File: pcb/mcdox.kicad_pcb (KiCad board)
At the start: 2 copper layers, 39 x 46 mm, 5 parts

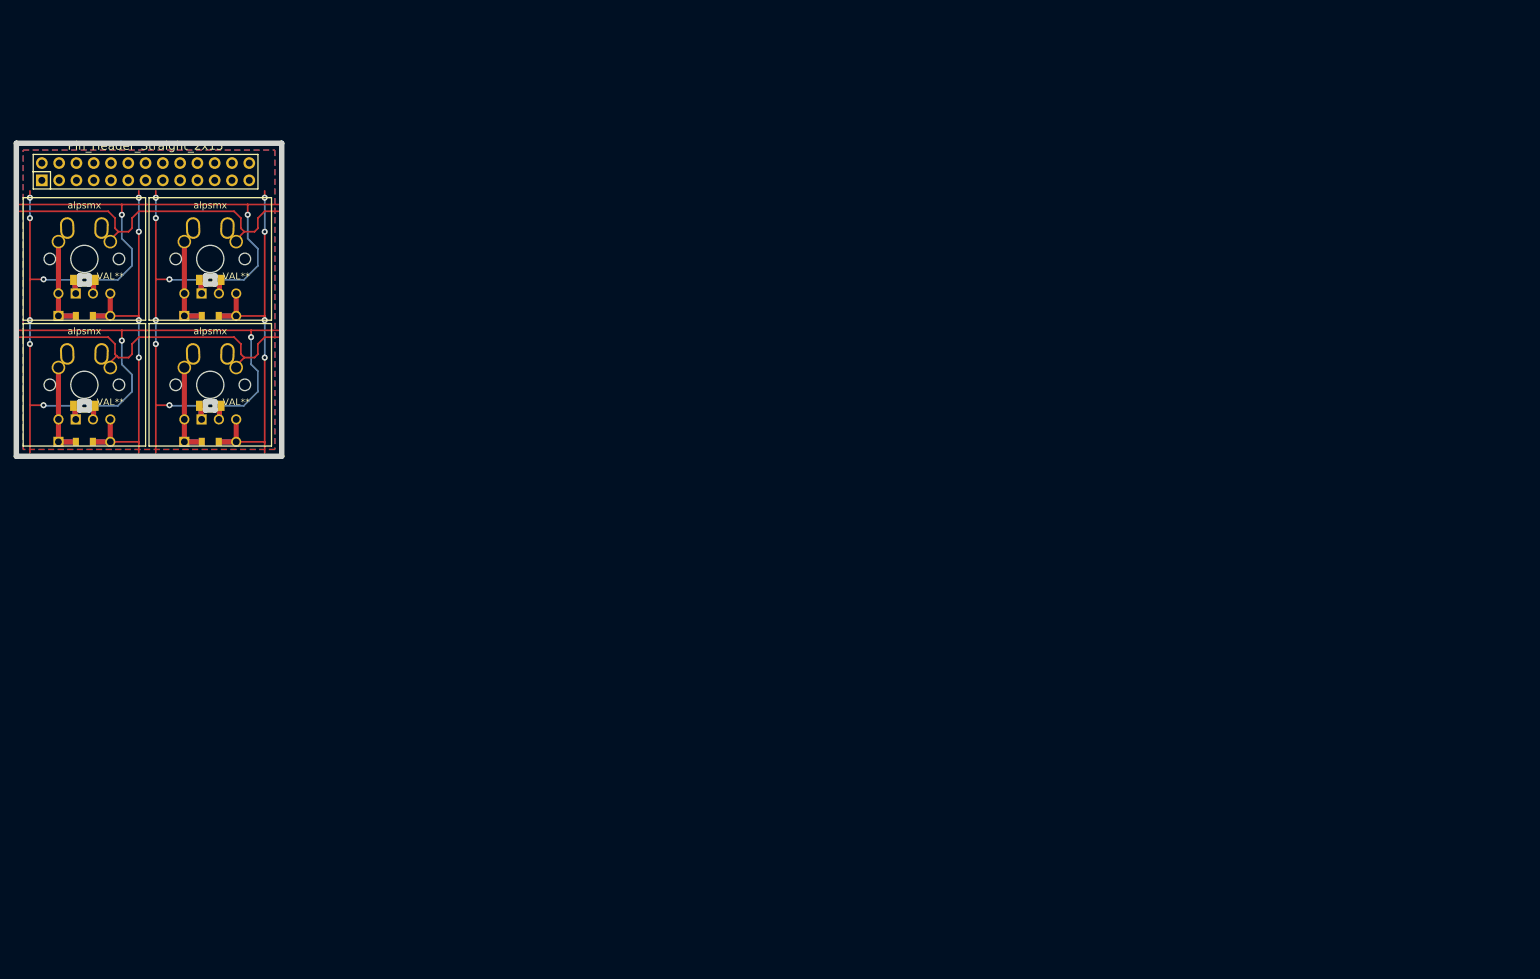
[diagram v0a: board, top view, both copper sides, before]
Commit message: First proper attempt at a full routing.
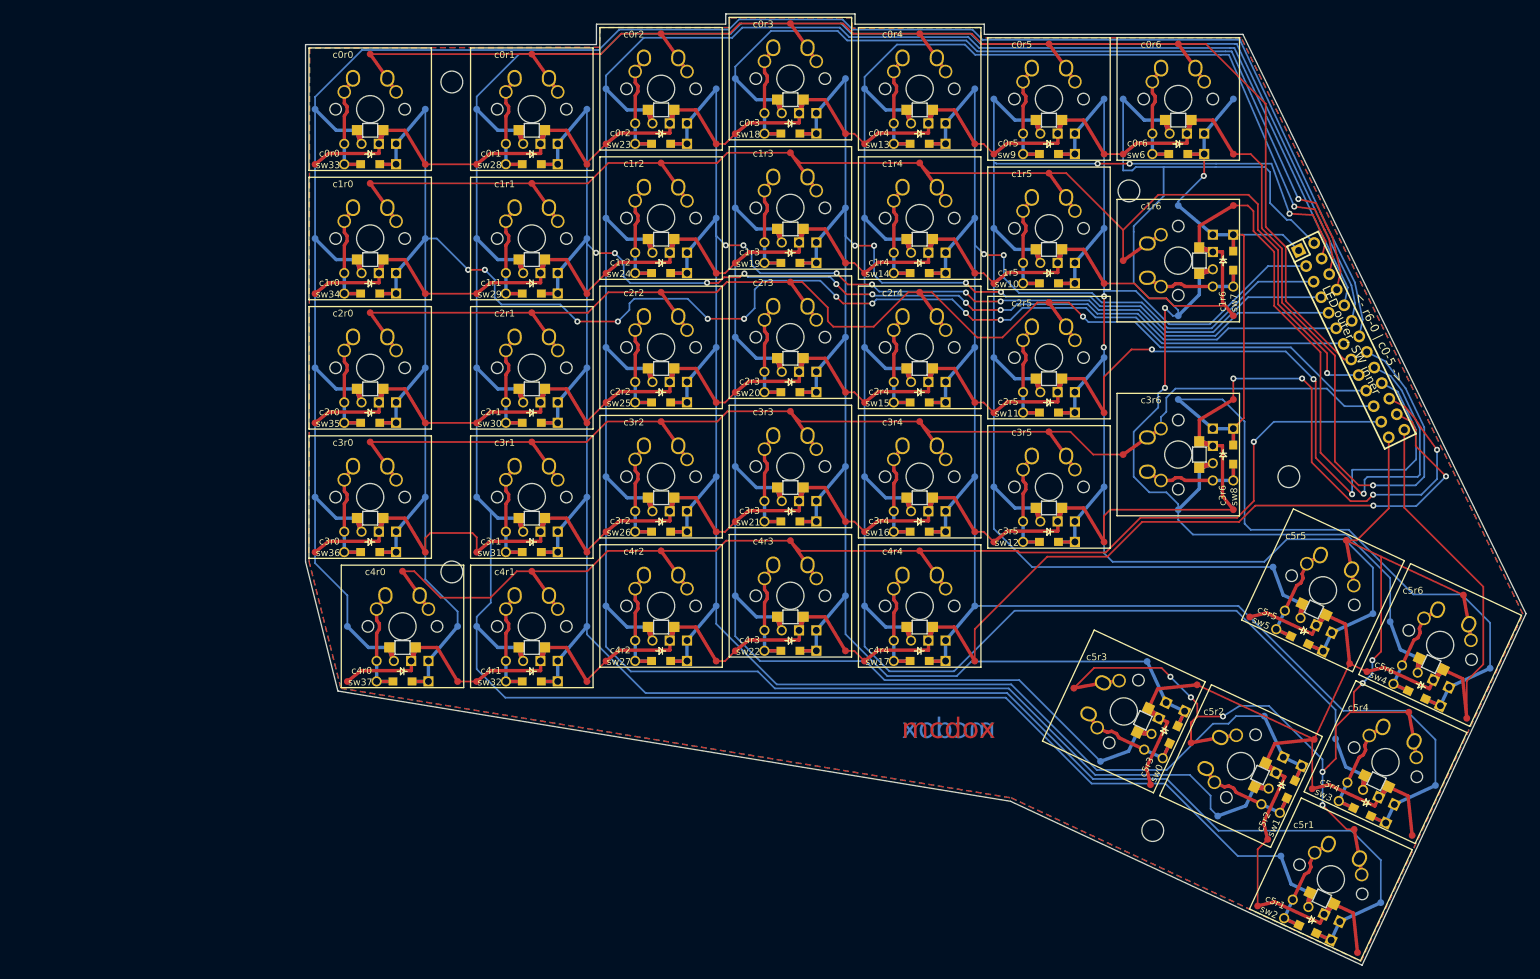
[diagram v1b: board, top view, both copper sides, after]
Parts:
- removed Pin_Header_Straight_2x13: Val**, Pin_Headers:Pin_Header_Straight_2x13
- removed alpsmx (x4): VAL**, mcdox:alpsmx
- added <- r6-0 | c0-5 ->: LED outer, SW inner, Pin_Header_Straight_2X13, F.Cu at (224.2, 67.9)
- added ?: , m3_hole, F.Cu at (92.0, 102.0)
- added ?: , m3_hole, F.Cu at (92.0, 30.0)
- added ?: , m3_hole, F.Cu at (191.5, 46.0)
- added ?: , m3_hole, F.Cu at (215.0, 88.0)
- added ?: , m3_hole, F.Cu at (195.0, 140.0)
- added sw0: c5r3, alpsmx, F.Cu at (190.8, 122.5)
- added sw1: c5r2, alpsmx, F.Cu at (208.0, 130.5)
- added sw10: c1r5, alpsmx, F.Cu at (179.8, 51.5)
- added sw11: c2r5, alpsmx, F.Cu at (179.8, 70.5)
- added sw12: c3r5, alpsmx, F.Cu at (179.8, 89.5)
- added sw13: c0r4, alpsmx, F.Cu at (160.8, 31.0)
- added sw14: c1r4, alpsmx, F.Cu at (160.8, 50.0)
- added sw15: c2r4, alpsmx, F.Cu at (160.8, 69.0)
- added sw16: c3r4, alpsmx, F.Cu at (160.8, 88.0)
- added sw17: c4r4, alpsmx, F.Cu at (160.8, 107.0)
- added sw18: c0r3, alpsmx, F.Cu at (141.8, 29.5)
- added sw19: c1r3, alpsmx, F.Cu at (141.8, 48.5)
- added sw2: c5r1, alpsmx, F.Cu at (221.2, 147.2)
- added sw20: c2r3, alpsmx, F.Cu at (141.8, 67.5)
- added sw21: c3r3, alpsmx, F.Cu at (141.8, 86.5)
- added sw22: c4r3, alpsmx, F.Cu at (141.8, 105.5)
- added sw23: c0r2, alpsmx, F.Cu at (122.8, 31.0)
- added sw24: c1r2, alpsmx, F.Cu at (122.8, 50.0)
- added sw25: c2r2, alpsmx, F.Cu at (122.8, 69.0)
- added sw26: c3r2, alpsmx, F.Cu at (122.8, 88.0)
- added sw27: c4r2, alpsmx, F.Cu at (122.8, 107.0)
- added sw28: c0r1, alpsmx, F.Cu at (103.8, 34.0)
- added sw29: c1r1, alpsmx, F.Cu at (103.8, 53.0)
- added sw3: c5r4, alpsmx, F.Cu at (229.2, 129.9)
- added sw30: c2r1, alpsmx, F.Cu at (103.8, 72.0)
- added sw31: c3r1, alpsmx, F.Cu at (103.8, 91.0)
- added sw32: c4r1, alpsmx, F.Cu at (103.8, 110.0)
- added sw33: c0r0, alpsmx, F.Cu at (80.0, 34.0)
- added sw34: c1r0, alpsmx, F.Cu at (80.0, 53.0)
- added sw35: c2r0, alpsmx, F.Cu at (80.0, 72.0)
- added sw36: c3r0, alpsmx, F.Cu at (80.0, 91.0)
- added sw37: c4r0, alpsmx, F.Cu at (84.8, 110.0)
- added sw4: c5r6, alpsmx, F.Cu at (237.2, 112.7)
- added sw5: c5r5, alpsmx, F.Cu at (220.0, 104.7)
- added sw6: c0r6, alpsmx, F.Cu at (198.8, 32.5)
- added sw7: c1r6, alpsmx, F.Cu at (198.8, 56.2)
- added sw8: c3r6, alpsmx, F.Cu at (198.8, 84.8)
- added sw9: c0r5, alpsmx, F.Cu at (179.8, 32.5)
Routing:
- net (no net): track 437.2 -> 5020.2 mm, vias 24 -> 61
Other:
- board size 39 x 46 mm -> 179.4 x 139.8 mm
- rule trace_min: 0.254 -> 0.5
- board text added: "c0r0"
- board text added: "c0r1"
- board text added: "c0r2"
- board text added: "c0r3"
- board text added: "c0r4"
- board text added: "c0r5"
- board text added: "c0r6"
- board text added: "c1r0"
- board text added: "c1r1"
- board text added: "c1r2"
- board text added: "c1r3"
- board text added: "c1r4"
- board text added: "c1r5"
- board text added: "c1r6"
- board text added: "c2r0"
- board text added: "c2r1"
- board text added: "c2r2"
- board text added: "c2r3"
- board text added: "c2r4"
- board text added: "c2r5"
- board text added: "c3r0"
- board text added: "c3r1"
- board text added: "c3r2"
- board text added: "c3r3"
- board text added: "c3r4"
- board text added: "c3r5"
- board text added: "c3r6"
- board text added: "c4r0"
- board text added: "c4r1"
- board text added: "c4r2"
- board text added: "c4r3"
- board text added: "c4r4"
- board text added: "c5r1"
- board text added: "c5r2"
- board text added: "c5r3"
- board text added: "c5r4"
- board text added: "c5r5"
- board text added: "c5r6"
- board text added: "mcdox"

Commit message: Move reference/value in footprint to make silkscreen nicer.
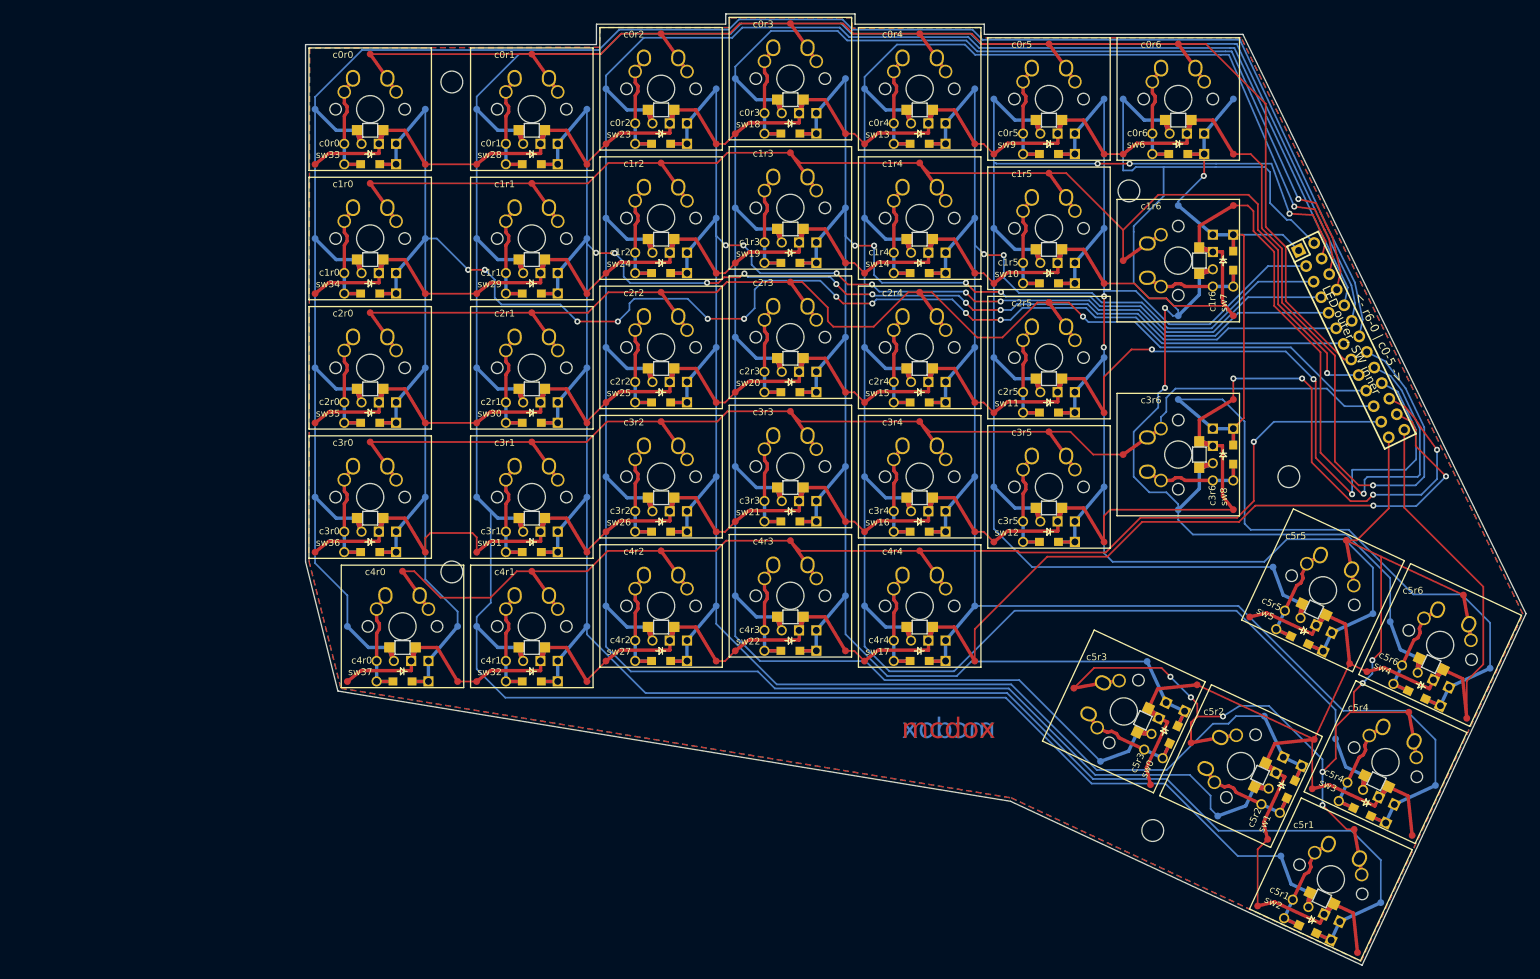
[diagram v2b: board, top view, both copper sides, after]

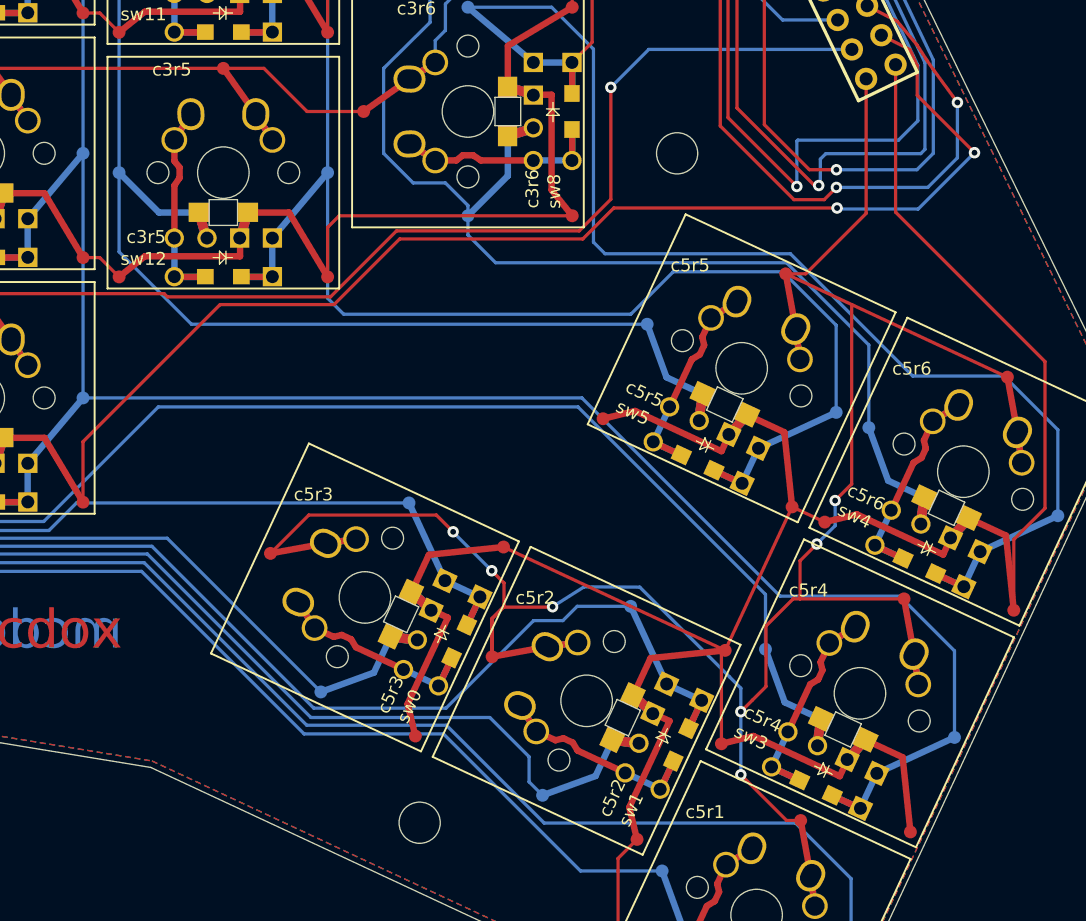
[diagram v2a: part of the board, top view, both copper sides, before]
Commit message: Tweaked PCB to match moved switch for smaller thumb keys.
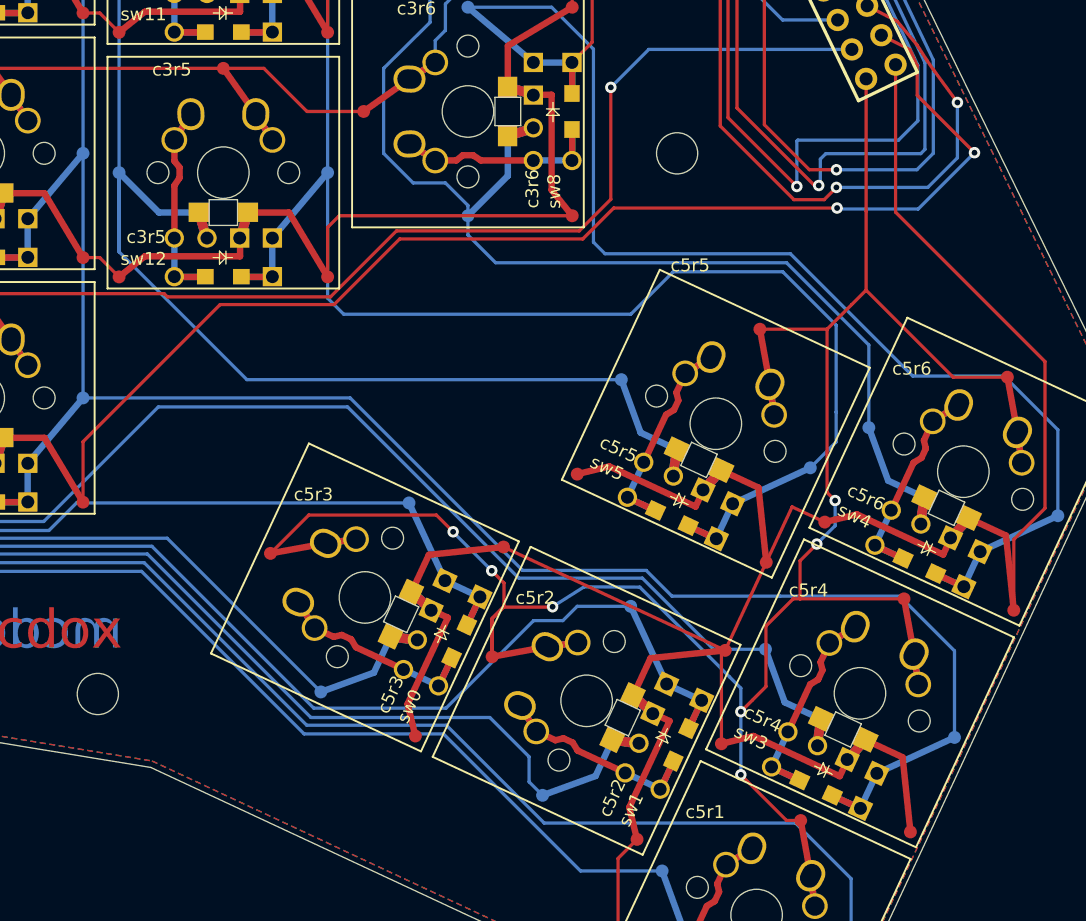
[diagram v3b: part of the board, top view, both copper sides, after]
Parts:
- moved ? 25.7 mm to (171.0, 130.9)
- moved sw5 4.75 mm to (218.0, 109.0)
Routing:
- net (no net): track 5020.2 -> 5028.7 mm
